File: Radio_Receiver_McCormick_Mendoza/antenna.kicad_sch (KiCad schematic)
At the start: 31 parts, among them J33 XFIL_IN, J34 XFIL_OUT, J45 CENTER_TAP, J5 Conn_Coaxial, J5 FIL_IN, J8 FIL_OUT, T1 Transformer_1P_SS, U13 SN74CBT3253CDBR

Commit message: Added MicroSD card and verified footprints
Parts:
- renumbered J5 to J47
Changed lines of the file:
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@@
 		(in_pos_files yes)
 		(dnp no)
-		(property "Reference" "J5"
+		(property "Reference" "J47"
 			(at 44.1452 36.4744 90)
 			(show_name no)
@@
 			(project "Radio_Receiver_McCormick_Mendoza"
 				(path "/f31d31ab-6846-4f3a-92b1-aa5a6a13373f/bb2f90fe-90d6-4041-8023-4e8a6153d0ef"
-					(reference "J5")
+					(reference "J47")
 					(unit 1)
 				)

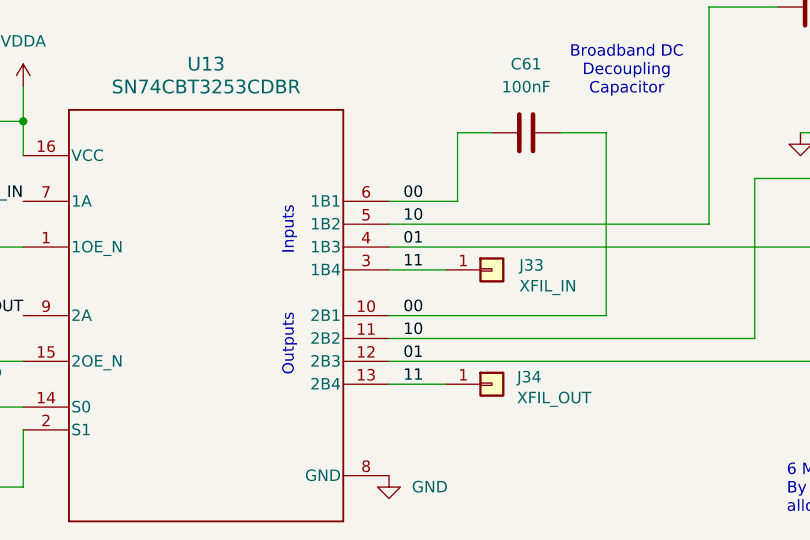
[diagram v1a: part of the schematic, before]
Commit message: Arranged antenna and mixer components on PCB
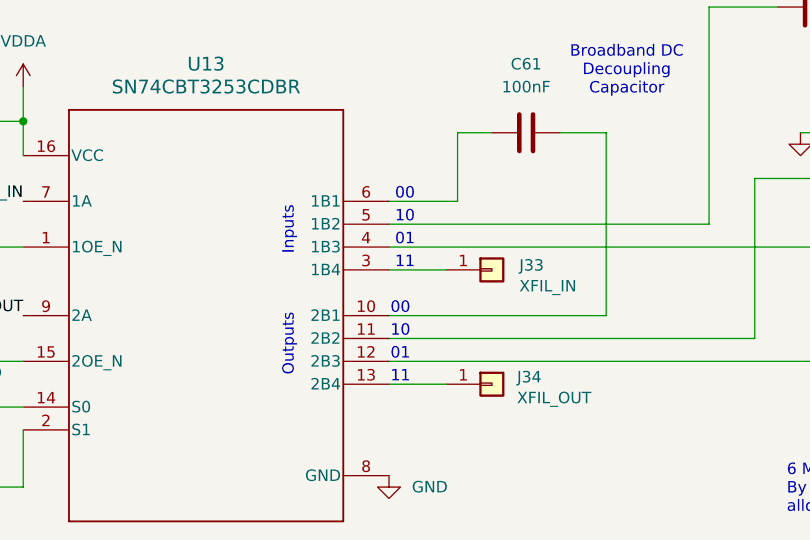
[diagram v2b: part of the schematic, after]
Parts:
- JP1: footprint Connector_PinHeader_2.54mm:PinHeader_1x02_P2.54mm_Vertical -> Jumper:SolderJumper-2_P1.3mm_Bridged2Bar_RoundedPad1.0x1.5mm
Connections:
- net 00: no longer names the net of C61.2, U13.10 (2B1)
- net 00: no longer C61.1, U13.6 (1B1)
- net 01: no longer names the net of L6.2, U13.12 (2B3)
- net 01: no longer C22.1, U13.4 (1B3)
- net 10: no longer names the net of C19.1, C31.1, C55.1, L4.2, U13.11 (2B2)
- net 10: no longer C67.1, U13.5 (1B2)
- net 11: no longer names the net of J33.1 (Pin_1), U13.3 (1B4)
- net 11: no longer J34.1 (Pin_1), U13.13 (2B4)
- new net: J34.1 (Pin_1), U13.13 (2B4)
- new net: C22.1, U13.4 (1B3)
- new net: C67.1, U13.5 (1B2)
- new net: C61.1, U13.6 (1B1)
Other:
- note added: "00"
- note added: "01"
- note added: "10"
- note added: "11"
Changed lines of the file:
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@@
 		)
 	)
+	(text "00"
+		(exclude_from_sim no)
+		(at 149.098 114.808 0)
+		(effects
+			(font
+				(size 1.27 1.27)
+			)
+		)
+	)
 	(text "T37-6 Toroid: \n[NUMBER] turns"
 		(exclude_from_sim no)
@@
 		)
 	)
+	(text "11"
+		(exclude_from_sim no)
+		(at 148.59 135.128 0)
+		(effects
+			(font
+				(size 1.27 1.27)
+			)
+		)
+	)
+	(text "01"
+		(exclude_from_sim no)
+		(at 149.098 119.888 0)
+		(effects
+			(font
+				(size 1.27 1.27)
+			)
+		)
+	)
 	(text "Blocking Capacitor to stop the DC from\ngetting to the antenna. "
 		(exclude_from_sim no)
@@
 		)
 	)
+	(text "01"
+		(exclude_from_sim no)
+		(at 148.59 132.588 0)
+		(effects
+			(font
+				(size 1.27 1.27)
+			)
+		)
+	)
 	(text "10 kHz - 2 MHz (3rd Order, Butterworth filter)\nWe rely on the fact that AM radio transmissions are strong.\nWe may need to put a large capacitor at the beginning if DC\noffsets become an issue."
 		(exclude_from_sim no)
@@
 		)
 	)
+	(text "11"
+		(exclude_from_sim no)
+		(at 149.098 122.428 0)
+		(effects
+			(font
+				(size 1.27 1.27)
+			)
+		)
+	)
+	(text "10"
+		(exclude_from_sim no)
+		(at 149.098 117.348 0)
+		(effects
+			(font
+				(size 1.27 1.27)
+			)
+		)
+	)
 	(text "T37-6 Toroid: \n[NUMBER] turns"
 		(exclude_from_sim no)
@@
 		)
 	)
+	(text "10"
+		(exclude_from_sim no)
+		(at 148.59 130.048 0)
+		(effects
+			(font
+				(size 1.27 1.27)
+			)
+		)
+	)
 	(text "UPDATE GND AND GNDA."
 		(exclude_from_sim no)
@@
 		)
 	)
+	(text "00"
+		(exclude_from_sim no)
+		(at 148.59 127.508 0)
+		(effects
+			(font
+				(size 1.27 1.27)
+			)
+		)
+	)
 	(text "6 MHz - 16 MHz (3rd Order, Series-First Bessel filter)\nBy doing Series-First, DC signals cannot pass through the capacitor (C2), \nallowing better control over the DC offset going into the op-amps"
 		(exclude_from_sim no)
@@
 		)
 	)
-	(label "11"
-		(at 151.13 123.19 180)
-		(effects
-			(font
-				(size 1.27 1.27)
-			)
-			(justify right bottom)
-		)
-	)
 	(label "Signal_OUT"
 		(at 106.68 128.27 180)
@@
 		)
 	)
-	(label "00"
-		(at 151.13 128.27 180)
-		(effects
-			(font
-				(size 1.27 1.27)
-			)
-			(justify right bottom)
-		)
-	)
-	(label "01"
-		(at 151.13 133.35 180)
-		(effects
-			(font
-				(size 1.27 1.27)
-			)
-			(justify right bottom)
-		)
-	)
 	(label "Signal_IN"
 		(at 106.68 115.57 180)
@@
 		)
 	)
-	(label "11"
-		(at 151.13 135.89 180)
-		(effects
-			(font
-				(size 1.27 1.27)
-			)
-			(justify right bottom)
-		)
-	)
-	(label "10"
-		(at 151.13 118.11 180)
-		(effects
-			(font
-				(size 1.27 1.27)
-			)
-			(justify right bottom)
-		)
-	)
-	(label "00"
-		(at 151.13 115.57 180)
-		(effects
-			(font
-				(size 1.27 1.27)
-			)
-			(justify right bottom)
-		)
-	)
 	(label "Signal_IN"
 		(at 82.55 40.64 0)
@@
 		)
 	)
-	(label "10"
-		(at 151.13 130.81 180)
-		(effects
-			(font
-				(size 1.27 1.27)
-			)
-			(justify right bottom)
-		)
-	)
-	(label "01"
-		(at 151.13 120.65 180)
-		(effects
-			(font
-				(size 1.27 1.27)
-			)
-			(justify right bottom)
-		)
-	)
 	(hierarchical_label "RF_IN1"
 		(shape output)
@@
 			)
 		)
-		(property "Footprint" "Connector_PinHeader_2.54mm:PinHeader_1x02_P2.54mm_Vertical"
+		(property "Footprint" "Jumper:SolderJumper-2_P1.3mm_Bridged2Bar_RoundedPad1.0x1.5mm"
 			(at 33.02 49.53 0)
 			(hide yes)

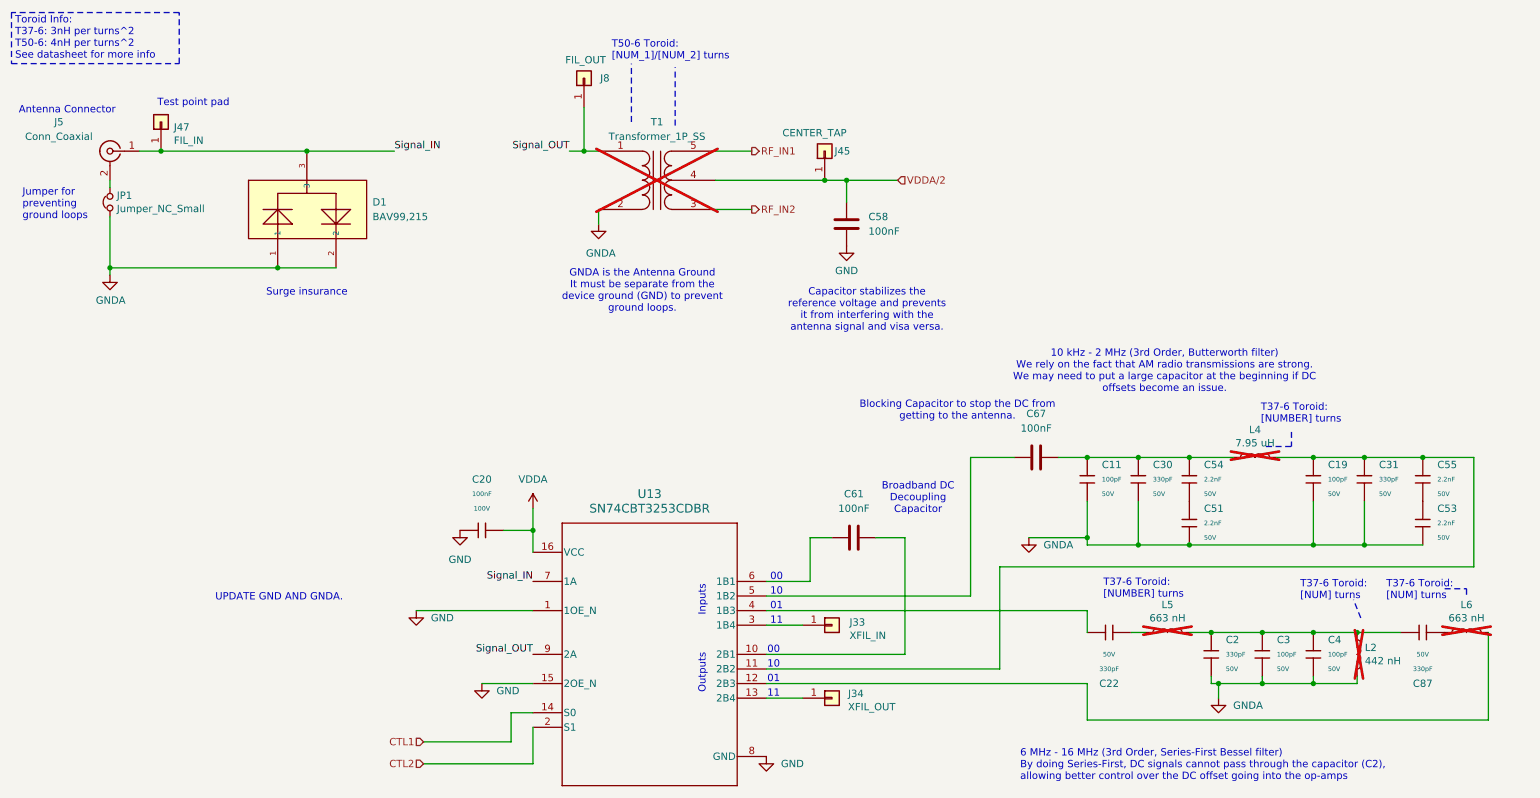
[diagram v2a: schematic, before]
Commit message: Routed antenna and isolated GNDA
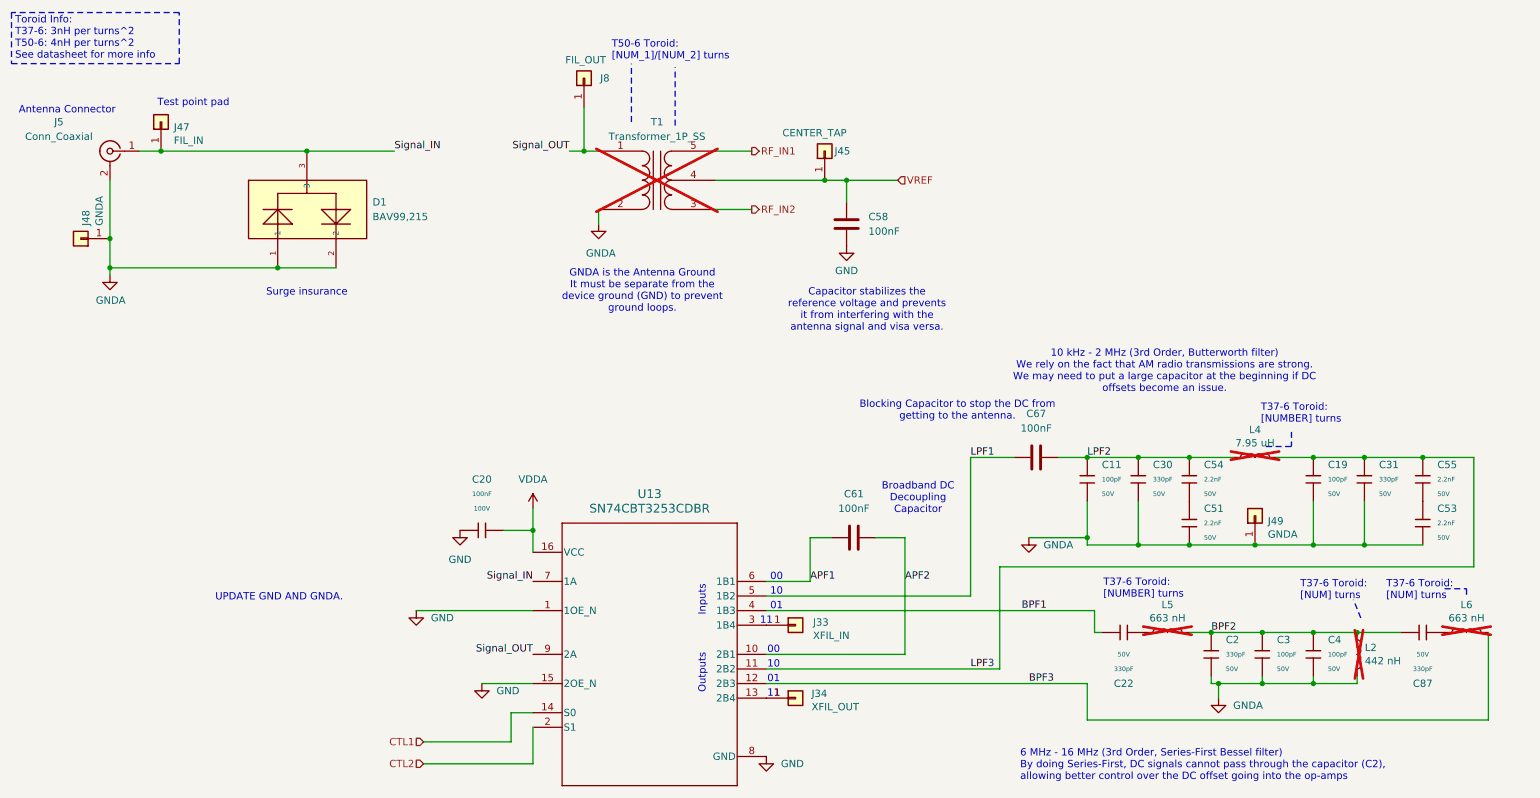
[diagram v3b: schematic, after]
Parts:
- removed JP1: Jumper_NC_Small, Jumper:SolderJumper-2_P1.3mm_Bridged2Bar_RoundedPad1.0x1.5mm, symbol SDRReciever-rescue:Jumper_NC_Small-Device-SDRReciever-rescue
- added J48, J49: GNDA, Connector_PinHeader_2.54mm:PinHeader_1x01_P2.54mm_Vertical, symbol SDRReciever-rescue:Conn_01x01-Connector_Generic-SDRReciever-rescue
- U13: footprint SN74CBT3253CDBR_1-4_MUX:DB0016A_N -> Reciever_Parts:DB0016A_N
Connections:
- net GNDA: now also J5.2 (Ext), J48.1 (Pin_1), J49.1 (Pin_1)
- net BPF2: now reaches C2.1, C3.1, C4.1, C87.1, L2.1, L5.2
- net LPF3: now reaches C19.1, C31.1, C55.1, L4.2, U13.11 (2B2)
- net BPF3: now reaches L6.2, U13.12 (2B3)
- net LPF2: now reaches C11.1, C30.1, C54.1, C67.2, L4.1
- net APF2: now reaches C61.2, U13.10 (2B1)
- net BPF1: now reaches C22.1, U13.4 (1B3)
- net LPF1: now reaches C67.1, U13.5 (1B2)
- net APF1: now reaches C61.1, U13.6 (1B1)
- net VDDA/2 renamed VREF
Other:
- note removed: "Jumper for preventing ground loops"
- moved on the sheet: C22, J33, J34

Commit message: Added Turn and Core type values to the hand-wound inductors and transformer
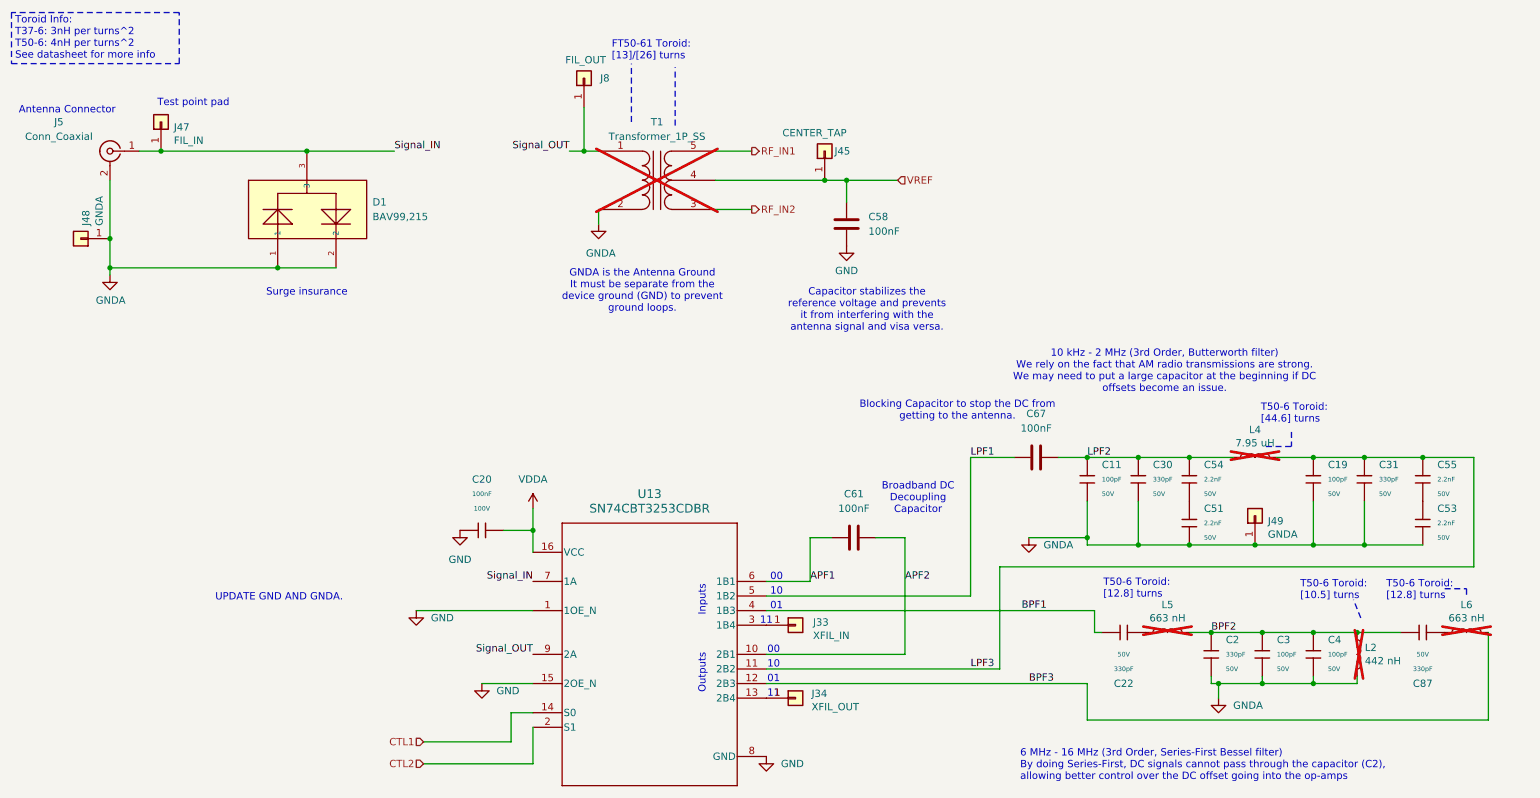
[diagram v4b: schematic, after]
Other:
- note added: "FT50-61 Toroid: [13]/[26] turns"
- note added: "T50-6 Toroid: [10.5] turns"
- note added: "T50-6 Toroid: [12.8] turns"
- note added: "T50-6 Toroid: [44.6] turns"
- note removed: "T37-6 Toroid: [NUMBER] turns"
- note removed: "T37-6 Toroid: [NUM] turns"
- note removed: "T50-6 Toroid: [NUM_1]/[NUM_2] turns"
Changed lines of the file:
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@@
 		)
 	)
-	(text "T50-6 Toroid: \n[NUM_1]/[NUM_2] turns"
+	(text "FT50-61 Toroid: \n[13]/[26] turns"
 		(exclude_from_sim no)
 		(at 120.396 24.892 0)
@@
 		)
 	)
-	(text "T37-6 Toroid: \n[NUMBER] turns"
+	(text "T50-6 Toroid: \n[44.6] turns"
 		(exclude_from_sim no)
 		(at 233.426 88.138 0)
@@
 		)
 	)
-	(text "T37-6 Toroid:\n[NUM] turns"
+	(text "T50-6 Toroid:\n[10.5] turns"
 		(exclude_from_sim no)
 		(at 240.284 118.872 0)
@@
 		)
 	)
-	(text "T37-6 Toroid: \n[NUMBER] turns"
+	(text "T50-6 Toroid: \n[12.8] turns"
 		(exclude_from_sim no)
 		(at 205.994 118.618 0)
@@
 		)
 	)
-	(text "T37-6 Toroid: \n[NUM] turns"
+	(text "T50-6 Toroid: \n[12.8] turns"
 		(exclude_from_sim no)
 		(at 255.27 118.872 0)

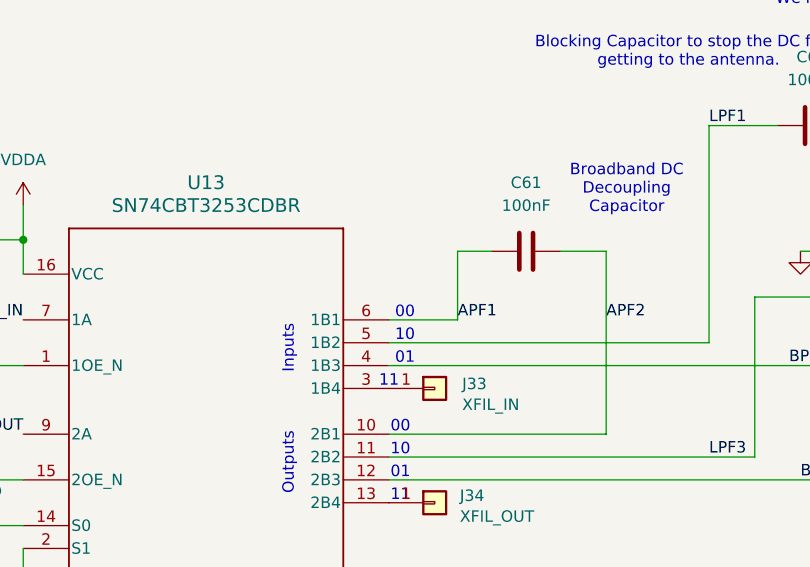
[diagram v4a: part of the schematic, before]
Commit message: Added Micropython files for board bring-up testing
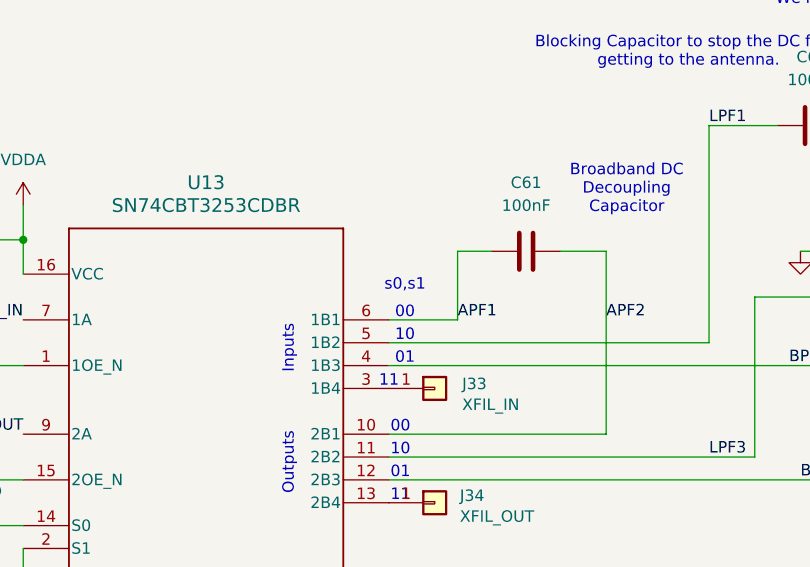
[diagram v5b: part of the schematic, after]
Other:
- note added: "s0,s1"
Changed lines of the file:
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@@
+		)
+	)
+	(text "s0,s1"
+		(exclude_from_sim no)
+		(at 149.098 111.76 0)
+		(effects
+			(font
+				(size 1.27 1.27)
+			)
 		)
 	)
